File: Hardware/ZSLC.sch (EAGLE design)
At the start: 22 parts, among them IC1 NAU7802-SOIC, J1 I2C, J22 DRDY, J3 X Load Cell, J4 Y Load Cell

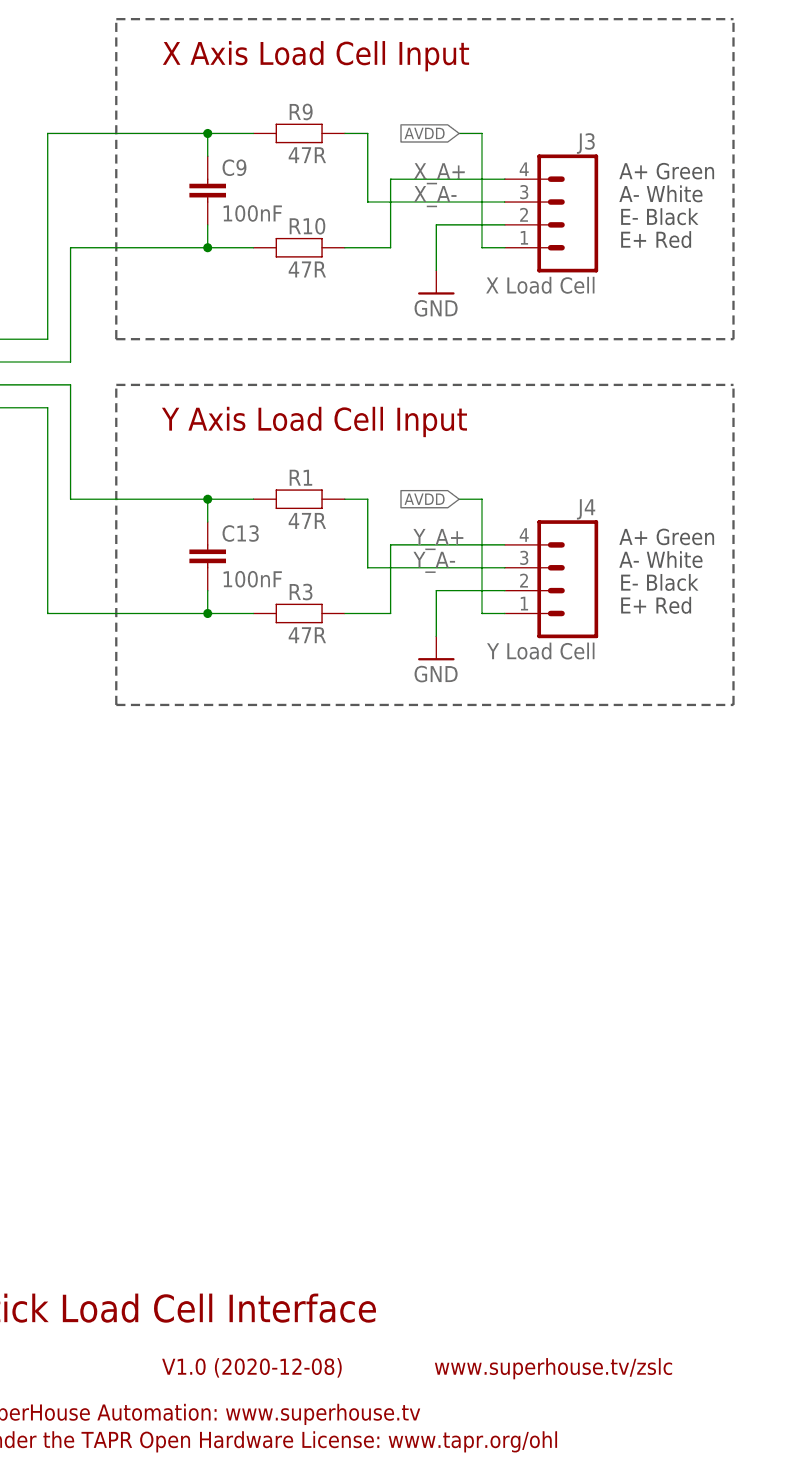
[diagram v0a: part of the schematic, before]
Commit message: Matched schematic input channel labels to PCB silkscreen.
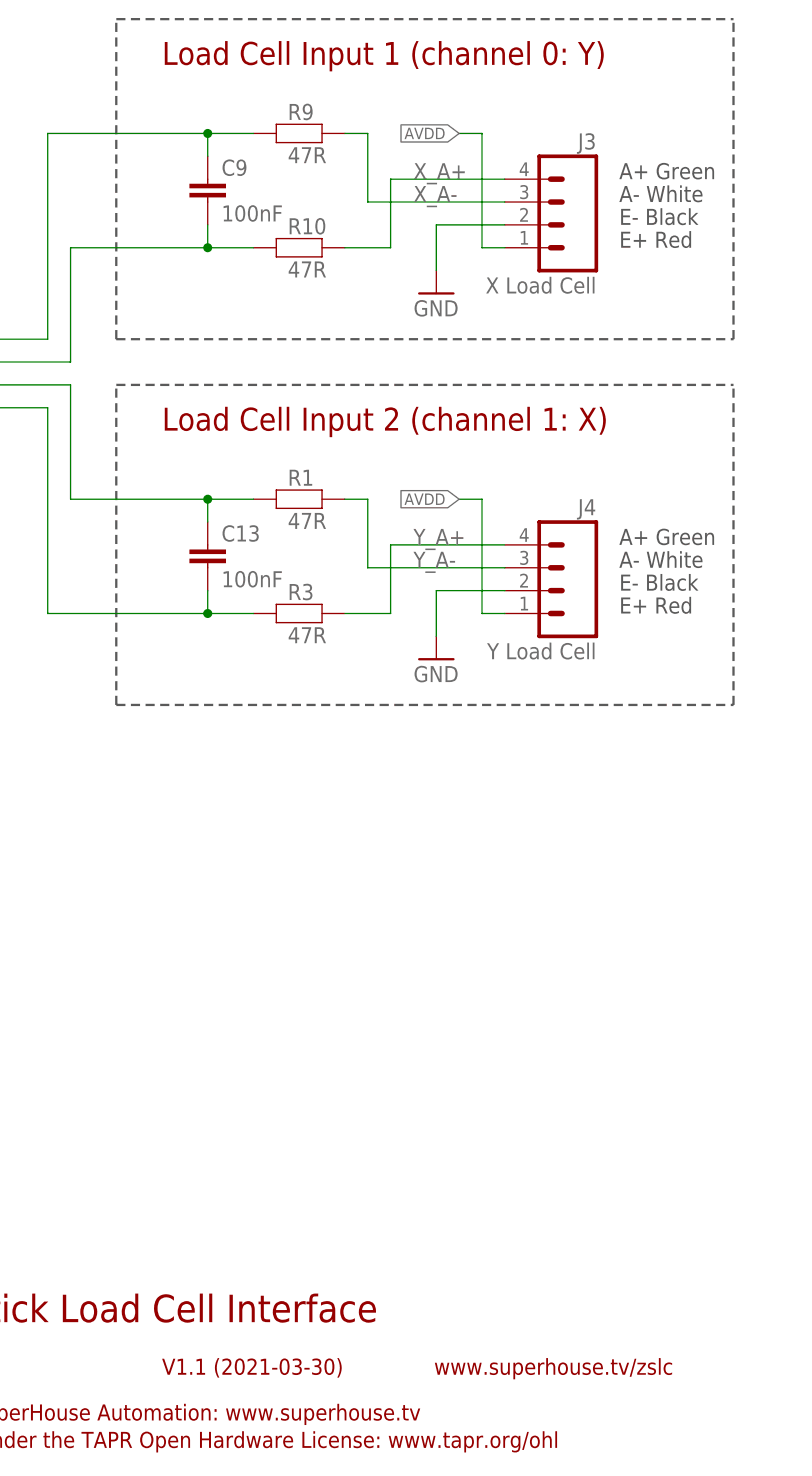
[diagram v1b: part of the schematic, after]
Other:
- note added: "Load Cell Input 1 (channel 0: Y)"
- note added: "Load Cell Input 2 (channel 1: X)"
- note added: "V1.1 (2021-03-30)"
- note removed: "V1.0 (2020-12-08)"
- note removed: "X Axis Load Cell Input"
- note removed: "Y Axis Load Cell Input"
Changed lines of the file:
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@@
 <frame x1="0" y1="0" x2="248.92" y2="185.42" columns="8" rows="5" layer="94"/>
 <text x="142.24" y="20.32" size="3.048" layer="94" font="vector">ZeroStick Load Cell Interface</text>
-<text x="172.72" y="14.478" size="1.778" layer="94">V1.0 (2020-12-08)</text>
+<text x="172.72" y="14.478" size="1.778" layer="94">V1.1 (2021-03-30)</text>
 <text x="142.24" y="14.478" size="1.778" layer="94">SKU: ZSLC</text>
 <text x="141.986" y="9.398" size="1.778" layer="94">(C)2020 SuperHouse Automation: www.superhouse.tv</text>
@@
 <wire x1="73.66" y1="20.32" x2="22.86" y2="20.32" width="0.254" layer="97" style="longdash"/>
 <wire x1="22.86" y1="20.32" x2="22.86" y2="68.58" width="0.254" layer="97" style="longdash"/>
-<text x="172.72" y="160.02" size="2.54" layer="94">X Axis Load Cell Input</text>
-<text x="172.72" y="119.38" size="2.54" layer="94">Y Axis Load Cell Input</text>
+<text x="172.72" y="160.02" size="2.54" layer="94">Load Cell Input 1 (channel 0: Y)</text>
+<text x="172.72" y="119.38" size="2.54" layer="94">Load Cell Input 2 (channel 1: X)</text>
 <text x="22.86" y="160.02" size="2.54" layer="94">I2C Header / Pullups</text>
 <text x="223.52" y="139.7" size="1.778" layer="97">E+ Red</text>

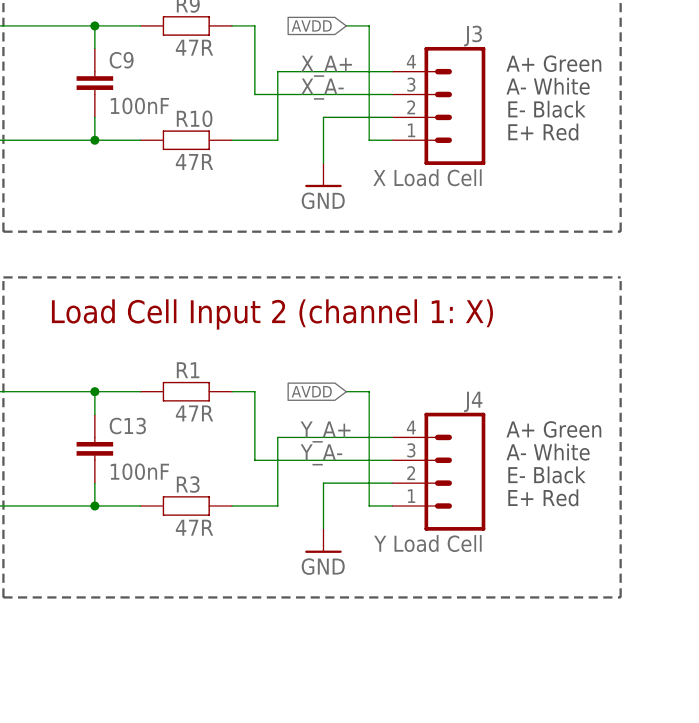
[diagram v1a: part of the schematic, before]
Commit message: Fixed labels and values on X and Y axis connectors.
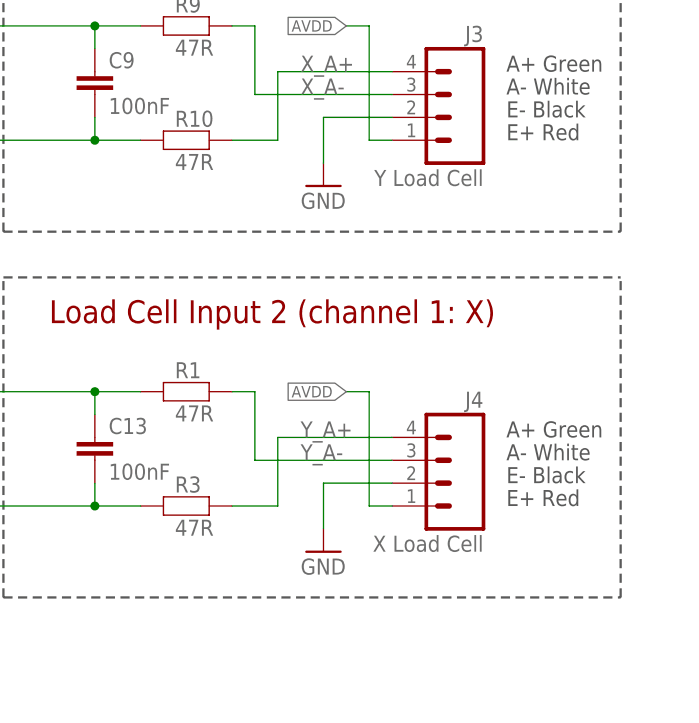
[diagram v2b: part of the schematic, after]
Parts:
- J3: value X Load Cell -> Y Load Cell
- J4: value Y Load Cell -> X Load Cell
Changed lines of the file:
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@@
 <part name="R7" library="SuperHouse-DiscreteSemi" library_urn="urn:adsk.eagle:library:11768461" deviceset="RESISTOR" device="0603" package3d_urn="urn:adsk.eagle:package:11768543/2" value="4K7"/>
 <part name="R8" library="SuperHouse-DiscreteSemi" library_urn="urn:adsk.eagle:library:11768461" deviceset="RESISTOR" device="0603" package3d_urn="urn:adsk.eagle:package:11768543/2" value="4K7"/>
-<part name="J3" library="SuperHouse-Connectors" library_urn="urn:adsk.eagle:library:11765989" deviceset="M04" device="-1.27-PLAIN" package3d_urn="urn:adsk.eagle:package:19968944/2" value="X Load Cell"/>
-<part name="J4" library="SuperHouse-Connectors" library_urn="urn:adsk.eagle:library:11765989" deviceset="M04" device="-1.27-PLAIN" package3d_urn="urn:adsk.eagle:package:19968944/2" value="Y Load Cell"/>
+<part name="J3" library="SuperHouse-Connectors" library_urn="urn:adsk.eagle:library:11765989" deviceset="M04" device="-1.27-PLAIN" package3d_urn="urn:adsk.eagle:package:19968944/2" value="Y Load Cell"/>
+<part name="J4" library="SuperHouse-Connectors" library_urn="urn:adsk.eagle:library:11765989" deviceset="M04" device="-1.27-PLAIN" package3d_urn="urn:adsk.eagle:package:19968944/2" value="X Load Cell"/>
 <part name="U$3" library="SuperHouse-Jumpers" library_urn="urn:adsk.eagle:library:12190622" deviceset="SJC" device="-NORMAL" package3d_urn="urn:adsk.eagle:package:7066342/2" value="SJC"/>
 <part name="U$4" library="SuperHouse-Jumpers" library_urn="urn:adsk.eagle:library:12190622" deviceset="SJC" device="-NORMAL" package3d_urn="urn:adsk.eagle:package:7066342/2" value="SJC"/>
